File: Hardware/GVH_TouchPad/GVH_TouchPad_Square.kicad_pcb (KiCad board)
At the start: 2 copper layers, 69.3 x 69.3 mm, 5 parts, among them J1 Conn_01x01, J2 Conn_01x01, J4 Conn_01x01, J5 Conn_01x01

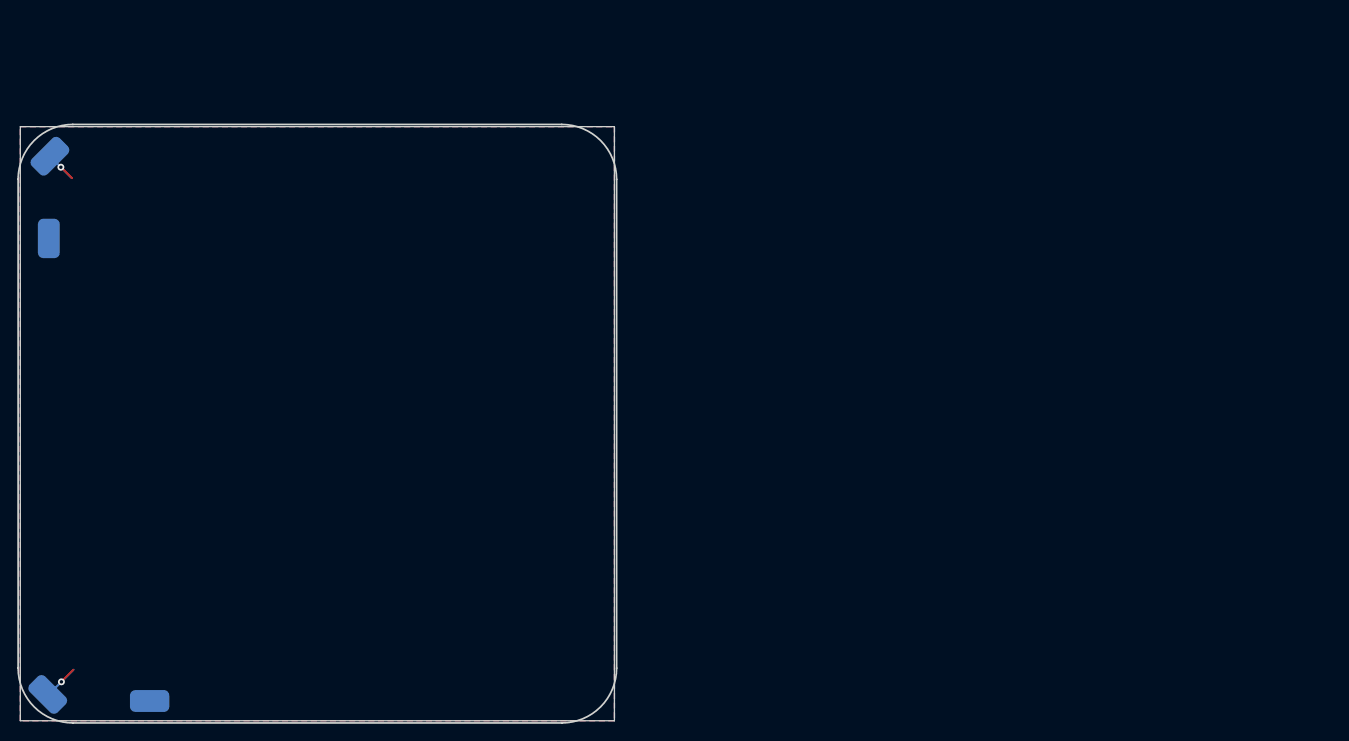
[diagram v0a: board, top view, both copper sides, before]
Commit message: Finished another layout. This is probably the one.
Also  finished the touch pad layouts
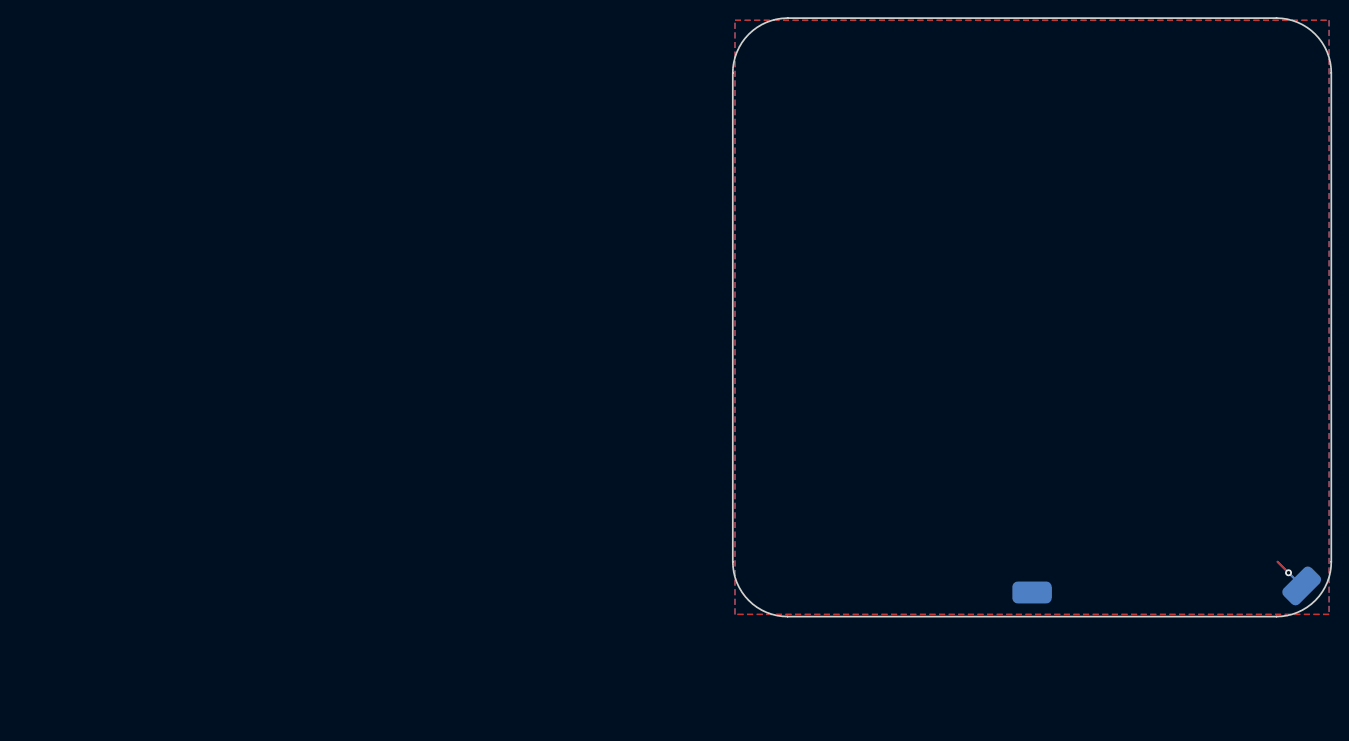
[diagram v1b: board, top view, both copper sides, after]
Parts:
- removed J2, J5: Conn_01x01, 0_touch_pad:SMD_Pad
- added G***: LOGO, 0_logo:MW_Logo_Horizontal_1.0inch, B.Cu at (218.6, 89.4)
- moved J4 145.8 mm to (250.1, 104.0), turned to 45 degrees
- moved J1 103.0 mm to (218.8, 104.8)
- moved REF** 83.3 mm to (218.6, 46.4)
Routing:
- net TOUCH: track 6.91 -> 3.41 mm, vias 2 -> 1
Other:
- outline, holes or cut-outs redrawn

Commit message: Layouts done and ordered.
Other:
- board text added: "GVH • Square Cap Touch Pad • V0.1 Daniel Bornhorst • 12/2024"
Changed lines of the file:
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@@
   (gr_arc (start 190.5 107.569) (mid 186.009872 105.709128) (end 184.15 101.219)
     (stroke (width 0.2) (type solid)) (layer "Edge.Cuts"))
+  (gr_text "GVH • Square Cap Touch Pad • V0.1\nDaniel Bornhorst • 12/2024" (at 218.567 95.377) (layer "B.SilkS")
+    (effects (font (size 1.016 1.016) (thickness 0.254) bold) (justify bottom mirror))
+  )
   (segment (start 248.539 102.489) (end 247.269 101.219) (width 0.254) (layer "F.Cu") (net 2))
   (via (at 248.539 102.489) (size 0.8) (drill 0.4) (layers "F.Cu" "B.Cu") (net 2))
